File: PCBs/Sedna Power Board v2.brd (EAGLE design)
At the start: 65 x 33.3 mm, 23 parts

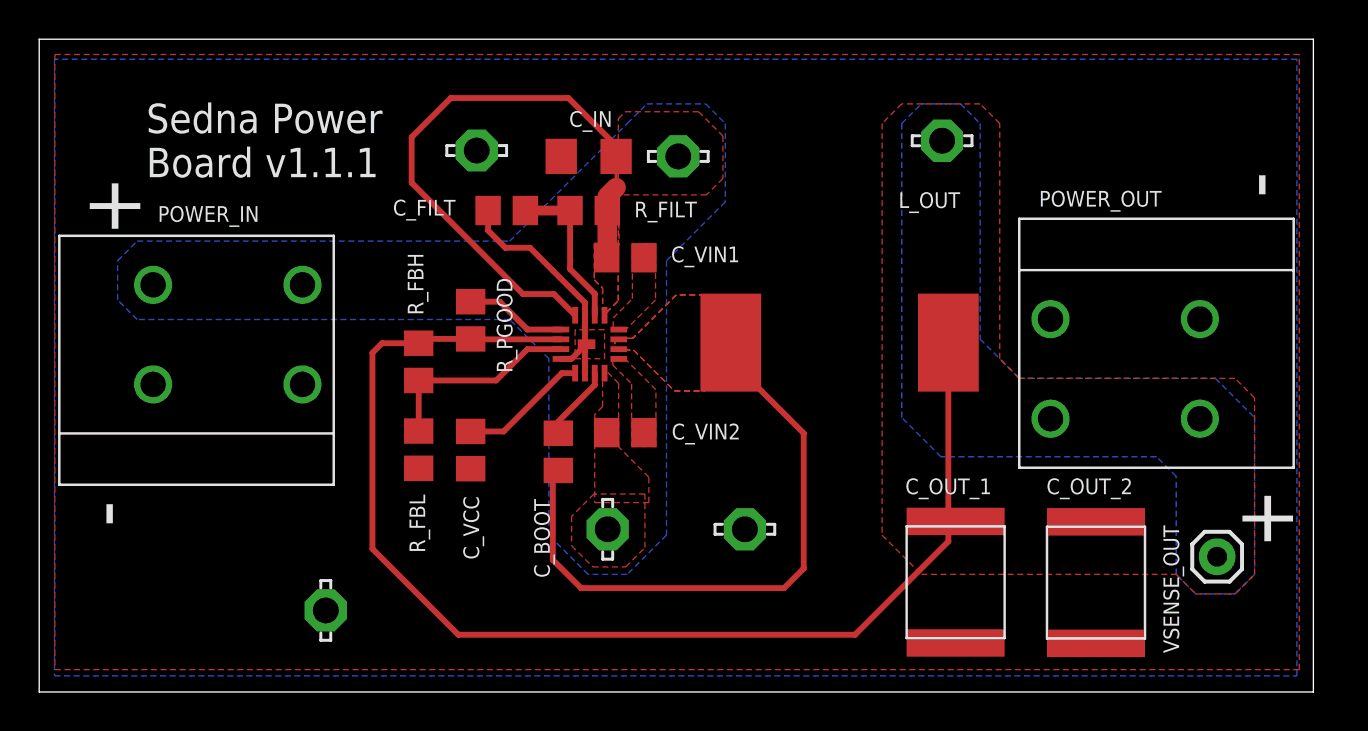
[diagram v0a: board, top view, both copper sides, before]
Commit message: Started working on v2 of the power board - double sided, smaller, should be much easier to etch and populate for a homebrew setup.
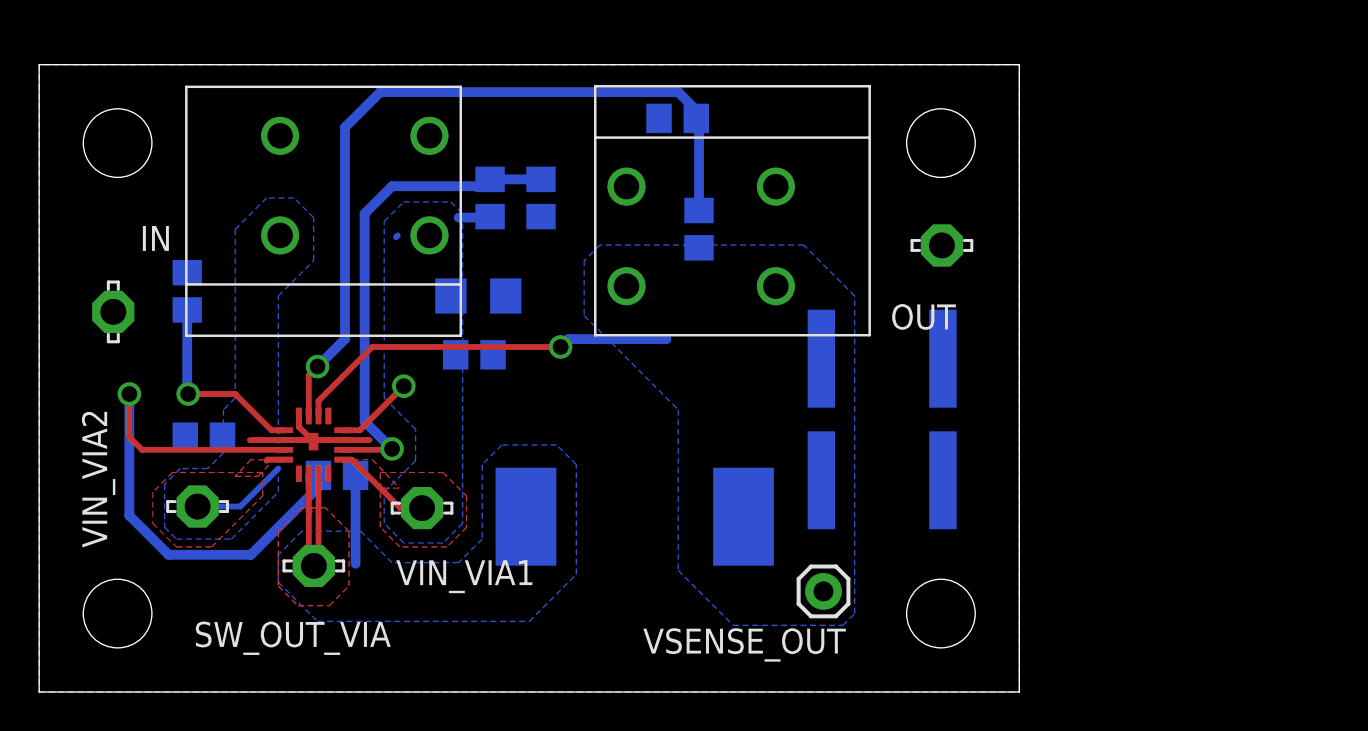
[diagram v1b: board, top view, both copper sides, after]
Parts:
- removed GND_VIA3, VOUT_VIA: LSP13, solpad:LSP13
- removed POWER_IN, POWER_OUT: EM279502V, Sedna Components:EM279502V
- removed R_PGOOD: 1000kΩ, rcl:R0805
- added IN: EM279502VALT_POLARITY, Sedna Components:EM279502V
- added OUT: EM279502V, Sedna Components:EM279502V
- added SW_OUT_VIA: LSP13, solpad:LSP13
- moved GND_VIA2 24.2 mm to (46.0, 22.8)
- moved VIN_VIA1 22.2 mm to (19.5, 9.38)
- moved C_VIN2 21.5 mm to (8.40, 13.0), flipped to the bottom
- moved R_FBL 21.5 mm to (32.6, 29.3), flipped to the bottom, turned to 0 degrees
- moved VIN_VIA2 21.0 mm to (8.08, 9.46), turned to 0 degrees
- moved VSENSE_OUT 20.2 mm to (40.0, 5.13), turned to 0 degrees
- moved GND_VIA1 18.7 mm to (3.78, 19.4)
- moved C_VCC 16.6 mm to (7.55, 20.4), flipped to the bottom, turned to 90 degrees
- moved R_FBH 15.8 mm to (33.7, 23.6), flipped to the bottom, turned to 90 degrees
- moved C_OUT_2 15.8 mm to (43.0, 17.0), flipped to the bottom, turned to 180 degrees
- moved REGULATOR 15.0 mm to (14.0, 12.6), turned to 0 degrees
- moved L_OUT 13.7 mm to (30.4, 8.94), flipped to the bottom, turned to 270 degrees
- moved C_BOOT 11.4 mm to (15.2, 11.1), flipped to the bottom, turned to 180 degrees
- moved C_VIN1 9.15 mm to (22.2, 17.2), flipped to the bottom, turned to 180 degrees
- moved C_IN 9.08 mm to (22.4, 20.2), flipped to the bottom
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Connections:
- removed net PGOOD_OUT: REGULATOR.5_PGOOD, R_PGOOD.1
- net GND: now also IN.1A, IN.1B, OUT.2A, OUT.2B; no longer GND_VIA3.MP, POWER_IN.2A, POWER_IN.2B, POWER_OUT.2A, POWER_OUT.2B
- net SW_OUT: now also SW_OUT_VIA.MP
- net V_IN: now also IN.2A, IN.2B; no longer POWER_IN.1A, POWER_IN.1B
- net V_OUT: now also OUT.1A, OUT.1B; no longer POWER_OUT.1A, POWER_OUT.1B, R_PGOOD.2, VOUT_VIA.MP
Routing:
- net V_OUT: track 63.2 -> 19.8 mm, vias 0 -> 1
- net FB: track 10.5 -> 40.2 mm, vias 0 -> 1
- net C_BOOT: track 3.84 -> 29.1 mm, vias 0 -> 1
- net SW_OUT: track 31.5 -> 14.2 mm
- net VINLDO: track 8.15 -> 24.9 mm, vias 0 -> 1
- net V_IN: track 31.6 -> 16.8 mm, vias 0 -> 1
- net PGOOD_OUT: track 5.19 -> 0.00 mm
- net GND: track 12.8 -> 7.72 mm
- net VCC: track 6.56 -> 10.0 mm, vias 0 -> 1
- added copper zone on layer 16, net SW_OUT
- removed copper zone on layer 1, net V_OUT
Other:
- board size 65 x 33.3 mm -> 50 x 32 mm
- board text added: "Sedna Power Board v2.0"
- board text removed: "Sedna Power Board v1.1.1"

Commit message: v2.0.2 of the power board - still prototyping, still learning...
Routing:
- net V_IN: track 16.8 -> 24.8 mm
- net V_OUT: track 19.8 -> 27.4 mm
- net VCC: track 10.0 -> 9.42 mm
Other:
- board text added: "Sedna Power Board v2.0.2"
- board text removed: "Sedna Power Board v2.0"
